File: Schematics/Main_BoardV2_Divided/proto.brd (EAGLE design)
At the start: 485.1 x 347.6 mm, 287 parts

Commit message: Routd and Cams Created
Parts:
- added CONTROL_LOGIC1:R22: 220, rcl:0204/7
- moved PROGRAM-COUNTER1:LED1 15.2 mm to (210.8, 365.8)
- moved PROGRAM-COUNTER1:LED10 15.2 mm to (210.8, 308.6)
- moved PROGRAM-COUNTER1:LED11 15.2 mm to (210.8, 302.3)
- moved PROGRAM-COUNTER1:LED12 15.2 mm to (210.8, 295.9)
- moved PROGRAM-COUNTER1:LED13 15.2 mm to (210.8, 289.6)
- moved PROGRAM-COUNTER1:LED14 15.2 mm to (210.8, 283.2)
- moved PROGRAM-COUNTER1:LED15 15.2 mm to (210.8, 276.9)
- moved PROGRAM-COUNTER1:LED16 15.2 mm to (210.8, 270.5)
- moved PROGRAM-COUNTER1:LED2 15.2 mm to (210.8, 359.4)
- moved PROGRAM-COUNTER1:LED3 15.2 mm to (210.8, 353.1)
- moved PROGRAM-COUNTER1:LED4 15.2 mm to (210.8, 346.7)
- moved PROGRAM-COUNTER1:LED5 15.2 mm to (210.8, 340.4)
- moved PROGRAM-COUNTER1:LED6 15.2 mm to (210.8, 334.0)
- moved PROGRAM-COUNTER1:LED7 15.2 mm to (210.8, 327.7)
- moved PROGRAM-COUNTER1:LED8 15.2 mm to (210.8, 321.3)
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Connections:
- new net CONTROL_LOGIC1:N$27: CONTROL_LOGIC1:IC5.4, CONTROL_LOGIC1:IC5.5, CONTROL_LOGIC1:R22.2, CONTROL_LOGIC1:S1.1B
- net GND: now also CONTROL_LOGIC1:R22.1; no longer CONTROL_LOGIC1:IC5.4, CONTROL_LOGIC1:IC5.5, CONTROL_LOGIC1:S1.1B
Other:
- board size 485.1 x 347.6 mm -> 472.4 x 347.6 mm

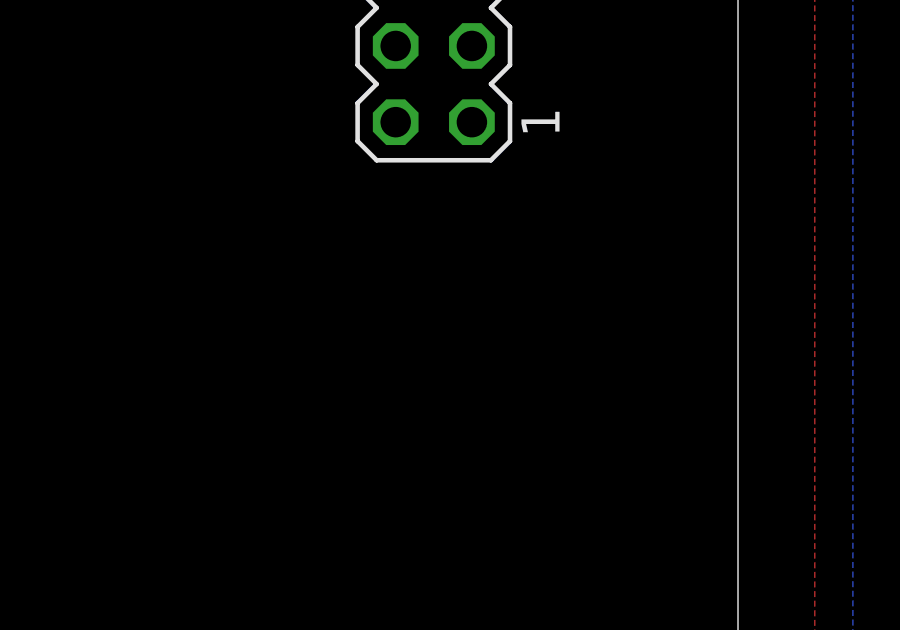
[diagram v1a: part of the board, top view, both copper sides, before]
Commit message: Microcode Added and Ram Updated
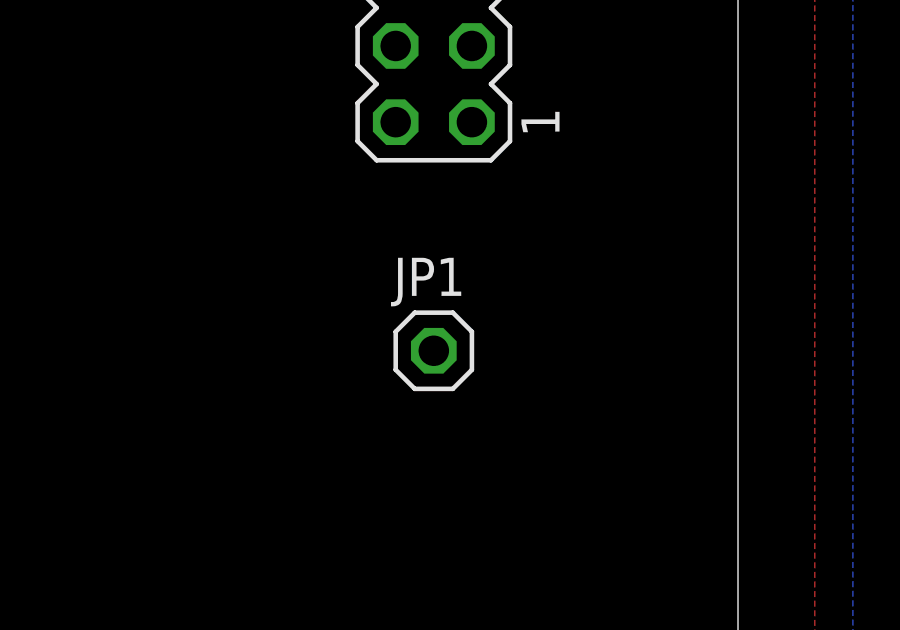
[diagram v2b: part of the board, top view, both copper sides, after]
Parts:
- added JP1: (no value), pinhead:1X01
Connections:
- new net NNOW2: JP1.1, RAM1:IC15.1, RAM1:IC16.1, RAM1:IC17.1, RAM1:IC18.1
- net SLC_ADDR: no longer RAM1:IC15.1, RAM1:IC16.1, RAM1:IC17.1, RAM1:IC18.1
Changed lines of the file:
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@@
 <attribute name="VALUE" x="367.9444" y="89.6874" size="0.9906" layer="27" ratio="10"/>
 </element>
+<element name="JP1" library="pinhead" library_urn="urn:adsk.eagle:library:325" package="1X01" package3d_urn="urn:adsk.eagle:package:22485/2" value="" x="407.67" y="237.49" smashed="yes">
+<attribute name="NAME" x="406.3238" y="239.3188" size="1.27" layer="25" ratio="10"/>
+<attribute name="VALUE" x="406.4" y="234.315" size="1.27" layer="27"/>
+</element>
 </elements>
 <signals>
@@
 <contactref element="RAM1:V1" pad="1"/>
 <contactref element="RAM1:V1" pad="4"/>
-<contactref element="RAM1:IC15" pad="1"/>
-<contactref element="RAM1:IC16" pad="1"/>
-<contactref element="RAM1:IC17" pad="1"/>
-<contactref element="RAM1:IC18" pad="1"/>
 <contactref element="CONTROL_LOGIC1:IC2" pad="10"/>
 <contactref element="CONTROL_LOGIC1:LED20" pad="A"/>
@@
 <wire x1="339.09" y1="121.92" x2="369.57" y2="114.3" width="0" layer="19" extent="1-1"/>
 <wire x1="252.73" y1="105.41" x2="339.09" y2="121.92" width="0" layer="19" extent="1-1"/>
-<wire x1="346.71" y1="248.92" x2="339.09" y2="121.92" width="0" layer="19" extent="1-1"/>
-<wire x1="365.76" y1="248.92" x2="346.71" y2="248.92" width="0" layer="19" extent="1-1"/>
-<wire x1="365.76" y1="275.59" x2="365.76" y2="248.92" width="0" layer="19" extent="1-1"/>
-<wire x1="346.71" y1="275.59" x2="365.76" y2="275.59" width="0" layer="19" extent="1-1"/>
-<wire x1="321.31" y1="307.34" x2="346.71" y2="275.59" width="0" layer="19" extent="1-1"/>
+<wire x1="321.31" y1="307.34" x2="339.09" y2="121.92" width="0" layer="19" extent="1-1"/>
 <wire x1="321.31" y1="314.96" x2="321.31" y2="307.34" width="0" layer="19" extent="1-1"/>
 <wire x1="273.05" y1="349.25" x2="321.31" y2="314.96" width="0" layer="19" extent="1-1"/>
@@
 <wire x1="294.64" y1="127" x2="294.64" y2="124.46" width="0" layer="19" extent="1-1"/>
 </signal>
+<signal name="NNOW2">
+<contactref element="RAM1:IC15" pad="1"/>
+<contactref element="RAM1:IC16" pad="1"/>
+<contactref element="RAM1:IC17" pad="1"/>
+<contactref element="RAM1:IC18" pad="1"/>
+<contactref element="JP1" pad="1"/>
+<wire x1="346.71" y1="275.59" x2="365.76" y2="275.59" width="0" layer="19" extent="1-1"/>
+<wire x1="365.76" y1="248.92" x2="365.76" y2="275.59" width="0" layer="19" extent="1-1"/>
+<wire x1="346.71" y1="248.92" x2="365.76" y2="248.92" width="0" layer="19" extent="1-1"/>
+<wire x1="407.67" y1="237.49" x2="346.71" y2="248.92" width="0" layer="19" extent="1-1"/>
+</signal>
 </signals>

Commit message: Bin Added and Sch Fixed
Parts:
- removed CLK1:IC2: 74AC11004, 74ac-logic:DIL20
- removed CLK1:IC6: 74AC11032, 74ac-logic:DIL16
- added CLK1:V1: 7404N, 74ttl-din:DIL14
- added CLK1:V2: 7432N, 74ttl-din:DIL14
- moved BUS1:11 294.6 mm to (-196.8, 416.6), flipped to the bottom
- moved BUS1:L8 289.6 mm to (-194.3, 421.6), flipped to the bottom
- moved BUS1:R16 284.6 mm to (-191.8, 426.7), flipped to the bottom
- moved BUS1:12 274.6 mm to (-186.7, 416.6), flipped to the bottom
- moved BUS1:L7 269.6 mm to (-184.2, 421.6), flipped to the bottom
- moved BUS1:R15 264.6 mm to (-181.6, 426.7), flipped to the bottom
- moved BUS1:13 254.6 mm to (-176.5, 416.6), flipped to the bottom
- moved BUS1:L6 249.6 mm to (-174.0, 421.6), flipped to the bottom
- moved BUS1:R14 244.6 mm to (-171.4, 426.7), flipped to the bottom
- moved BUS1:15 234.6 mm to (-166.4, 416.6), flipped to the bottom
- moved BUS1:L5 229.6 mm to (-163.8, 421.6), flipped to the bottom
- moved BUS1:R13 224.7 mm to (-161.3, 426.7), flipped to the bottom
- moved SV1 224.7 mm to (-161.3, 408.9), flipped to the bottom
- moved SV10 224.7 mm to (-161.3, 383.5), flipped to the bottom
- moved SV11 224.7 mm to (-161.3, 335.3), flipped to the bottom
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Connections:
- new net CLK1:+UB: CLK1:V1.14, CLK1:V2.14
- new net CLK1:-UB: CLK1:V1.7, CLK1:V2.7
- net 16BBUS1:VCC: now also 16BBUS1:D1.3, 16BBUS1:D1.5, 16BBUS1:D1.8, 16BBUS1:D2.3, 16BBUS1:D2.5, 16BBUS1:D2.8, 16BBUS1:D3.3, 16BBUS1:D3.5, 16BBUS1:D3.8, 16BBUS1:D4.3, 16BBUS1:D4.5, 16BBUS1:D4.8
- net CLK1:AMS: now also CLK1:IC1.2, CLK1:V1.1; no longer CLK1:IC1.5
- net CLK1:MCLK: now also CLK1:IC1.5; no longer CLK1:IC1.2, CLK1:IC2.20
- net CLK1:N$12: now also CLK1:V2.2; no longer CLK1:IC6.16
- net CLK1:N$13: now also CLK1:V2.1; no longer CLK1:IC6.1
- net CLK1:N$14: now also CLK1:V2.3; no longer CLK1:IC6.2
- net CLK1:N$17: now also CLK1:V1.2; no longer CLK1:IC2.1
- net CLK1:N$8: now also CLK1:V1.4; no longer CLK1:IC2.2
- net GND: no longer 16BBUS1:D1.3, 16BBUS1:D1.5, 16BBUS1:D1.8, 16BBUS1:D2.3, 16BBUS1:D2.5, 16BBUS1:D2.8, 16BBUS1:D3.3, 16BBUS1:D3.5, 16BBUS1:D3.8, 16BBUS1:D4.3, 16BBUS1:D4.5, 16BBUS1:D4.8, CLK1:IC2.4, CLK1:IC2.5, CLK1:IC2.6, CLK1:IC2.7, CLK1:IC6.4, CLK1:IC6.5
- net HLT: now also CLK1:V1.3; no longer CLK1:IC2.19
- net VCC: no longer CLK1:IC2.15, CLK1:IC2.16, CLK1:IC6.12, CLK1:IC6.13
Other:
- board size 472.4 x 347.6 mm -> 623.5 x 380.7 mm
